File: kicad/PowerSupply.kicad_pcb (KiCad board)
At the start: 2 copper layers, 90 x 140 mm, 115 parts, among them J1 USB_A, J2 Display, Q1 MMBT3904, Q10 MMBT3904, Q11 MMBT3904, Q2 MMBT3904, Q3 MMBT3904, Q4 MMBT3904, Q5 MMBT3904, Q6 MMBT3904, Q7 MMBT3904, Q8 MMBT3904, Q9 MMBT3904, SW1 ENC0 (Voltage), SW2 ENC1 (Current), SW3 SW_DIP_x04, U1 OPA4196, U10 STM32F373C8Tx, U2 OPA4196, U3 LD1086D2T33, U4 LD1086D2T33, U5 FQA36P15, U6 FQA36P15, U7 FQA36P15, U8 FQA36P15

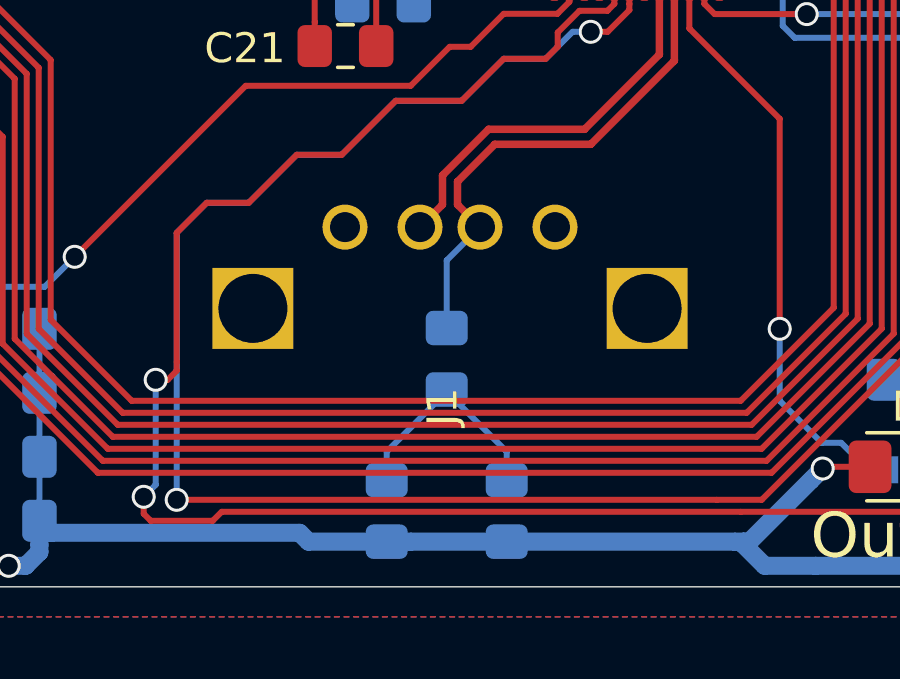
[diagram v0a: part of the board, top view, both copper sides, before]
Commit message: Fixed USB connector footprint, silkscreen was on mask layer
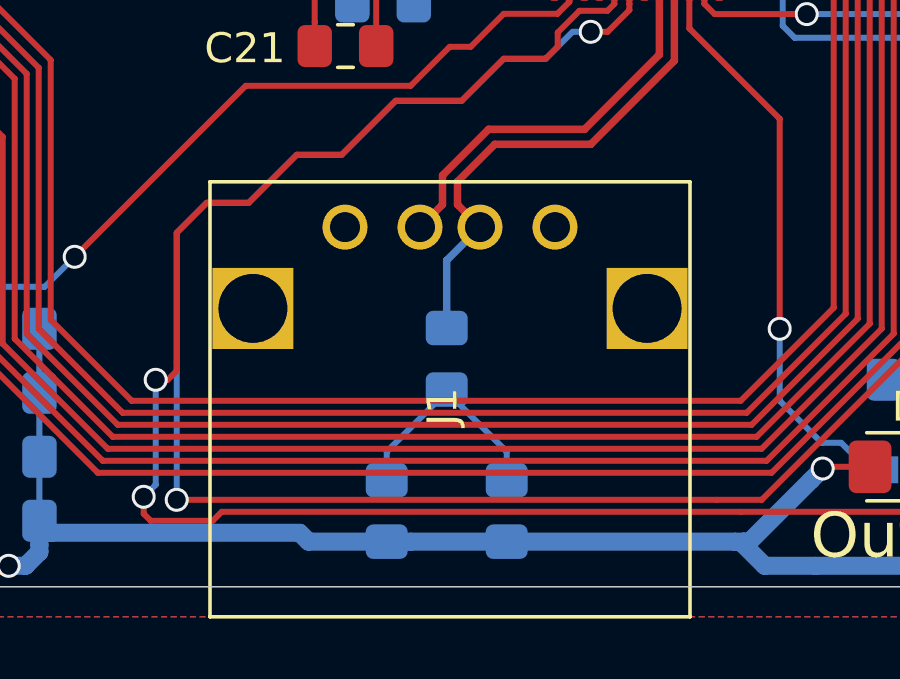
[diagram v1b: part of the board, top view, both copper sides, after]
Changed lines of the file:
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@@
       (effects (font (size 1 1) (thickness 0.15)))
     )
-    (fp_line (start 0 8) (end 14.5 8) (layer F.Mask) (width 0.12))
-    (fp_line (start 0 -8) (end 0 8) (layer F.Mask) (width 0.12))
-    (fp_line (start 14.5 -8) (end 0 -8) (layer F.Mask) (width 0.12))
-    (fp_line (start 14.5 -8) (end 14.5 8) (layer F.Mask) (width 0.12))
+    (fp_line (start 0 8) (end 14.5 8) (layer F.SilkS) (width 0.12))
+    (fp_line (start 0 -8) (end 0 8) (layer F.SilkS) (width 0.12))
+    (fp_line (start 14.5 -8) (end 0 -8) (layer F.SilkS) (width 0.12))
+    (fp_line (start 14.5 -8) (end 14.5 8) (layer F.SilkS) (width 0.12))
     (pad 4 thru_hole circle (at 12.99 3.5 90) (size 1.5 1.5) (drill 1) (layers *.Cu *.Mask)
       (net 1 GNDREF))
@@
   (segment (start 331.203554 125.25) (end 333.99 122.463554) (width 0.25) (layer F.Cu) (net 8))
   (segment (start 333.99 122.463554) (end 333.99 119.7325) (width 0.25) (layer F.Cu) (net 8))
-  (segment (start 326.4 129.12) (end 327.51 128.01) (width 0.2) (layer B.Cu) (net 8))
-  (segment (start 326.4 131.445) (end 326.4 129.12) (width 0.2) (layer B.Cu) (net 8))
+  (segment (start 326.4 129.12) (end 327.51 128.01) (width 0.25) (layer B.Cu) (net 8) (status 1000000))
+  (segment (start 326.4 131.445) (end 326.4 129.12) (width 0.25) (layer B.Cu) (net 8) (status 1000000))
   (segment (start 325.51 128.01) (end 326.26 127.26) (width 0.25) (layer F.Cu) (net 9))
   (segment (start 326.26 127.26) (end 326.26 126.286446) (width 0.25) (layer F.Cu) (net 9))
@@
   (segment (start 331.85 115.3) (end 333.8 113.35) (width 0.2) (layer F.Cu) (net 26))
   (segment (start 333.8 113.35) (end 334.2 113.35) (width 0.2) (layer F.Cu) (net 26))
-  (via (at 344.9 108) (size 0.8) (drill 0.6) (layers F.Cu B.Cu) (net 26) (status 1000000))
+  (via (at 344.9 108) (size 0.8) (drill 0.6) (layers F.Cu B.Cu) (net 26))
   (segment (start 344.825 108) (end 344.9 108) (width 0.2) (layer F.Cu) (net 26))
   (segment (start 329 92) (end 329 92.175) (width 0.2) (layer F.Cu) (net 26))

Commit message: git status
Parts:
- C1, C10, C11, C12, C13, C14, C15, C16, C17, C18, C19, C2, C20, C21, C22, C23, C24, C25, C26, C3, C4, C5, C6, C7, C8, C9: footprint Resistor_SMD:R_0805_2012Metric_Pad1.15x1.40mm_HandSolder -> Capacitor_SMD:C_0805_2012Metric_Pad1.15x1.40mm_HandSolder
- U5, U6, U7, U8: value FQA36P15 -> FQP17P10; footprint Package_TO_SOT_THT:TO-3P-3_Vertical -> Package_TO_SOT_THT:TO-220-3_Vertical
- moved U5 2.96 mm to (364.0, 105.5)
- moved U6 2.96 mm to (364.0, 47.5)
- moved U7 2.96 mm to (364.0, 76.5)
- moved U8 2.96 mm to (364.0, 18.5)
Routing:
- net /PassElement/Vin: track 270.4 -> 282.5 mm
- net /PassElement/Vout: track 326.9 -> 332.6 mm
- net /PassElement/VReg_set: track 110.3 -> 112.9 mm
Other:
- board text added: "Current"
- board text added: "Voltage"

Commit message: IDK what this is but the last commit message should've been FUCK I don't remember. BRUH
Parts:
- removed the REF** at (304.8, 26.5)
- removed the REF** at (304.8, 15.5)
- removed the REF** at (304.5, 4.50)
- added REF**: SolderWirePad_1x01_Drill2mm, Connector_Wire:SolderWirePad_1x01_Drill2mm, F.Cu at (4.75, 26.5)
- added REF**: SolderWirePad_1x01_Drill2mm, Connector_Wire:SolderWirePad_1x01_Drill2mm, F.Cu at (4.75, 15.5)
- added REF**: SolderWirePad_1x01_Drill2mm, Connector_Wire:SolderWirePad_1x01_Drill2mm, F.Cu at (4.50, 4.50)
- moved C1 300.0 mm to (31.0, 59.2)
- moved C10 300.0 mm to (67.0, 57.0)
- moved C11 300.0 mm to (10.0, 9.00)
- moved C12 300.0 mm to (39.8, 81.0)
- moved C13 300.0 mm to (30.3, 115.8)
- moved C14 300.0 mm to (32.7, 115.8)
- moved C15 300.0 mm to (35.1, 115.8)
- moved C16 300.0 mm to (24.2, 118.4)
- moved C17 300.0 mm to (24.2, 116.0)
- moved C18 300.0 mm to (24.3, 120.5)
- moved C19 300.0 mm to (23.0, 117.2)
- moved C2 300.0 mm to (31.0, 80.8)
- moved C20 300.0 mm to (23.0, 119.6)
- moved C21 300.0 mm to (23.0, 122.0)
- moved C22 300.0 mm to (37.6, 109.8)
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
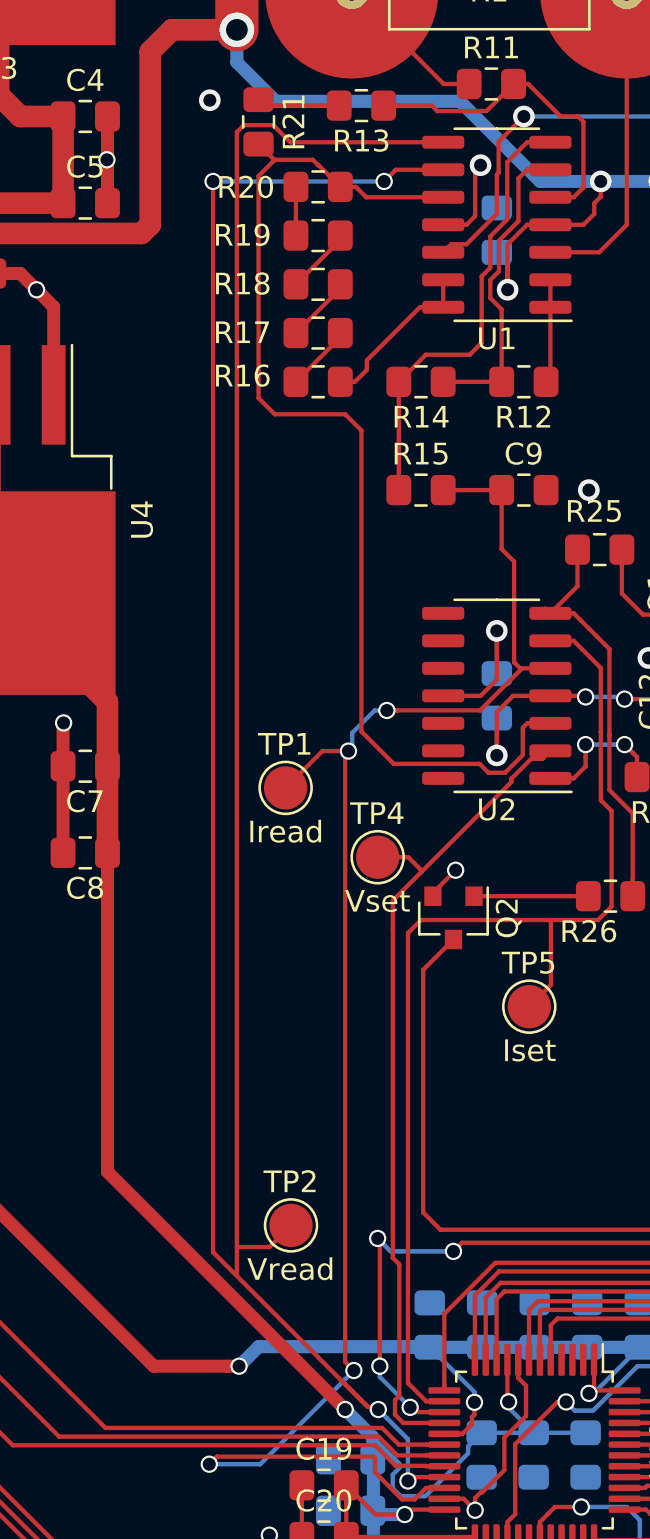
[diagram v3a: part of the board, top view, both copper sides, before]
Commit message: Removed unnecessary trace
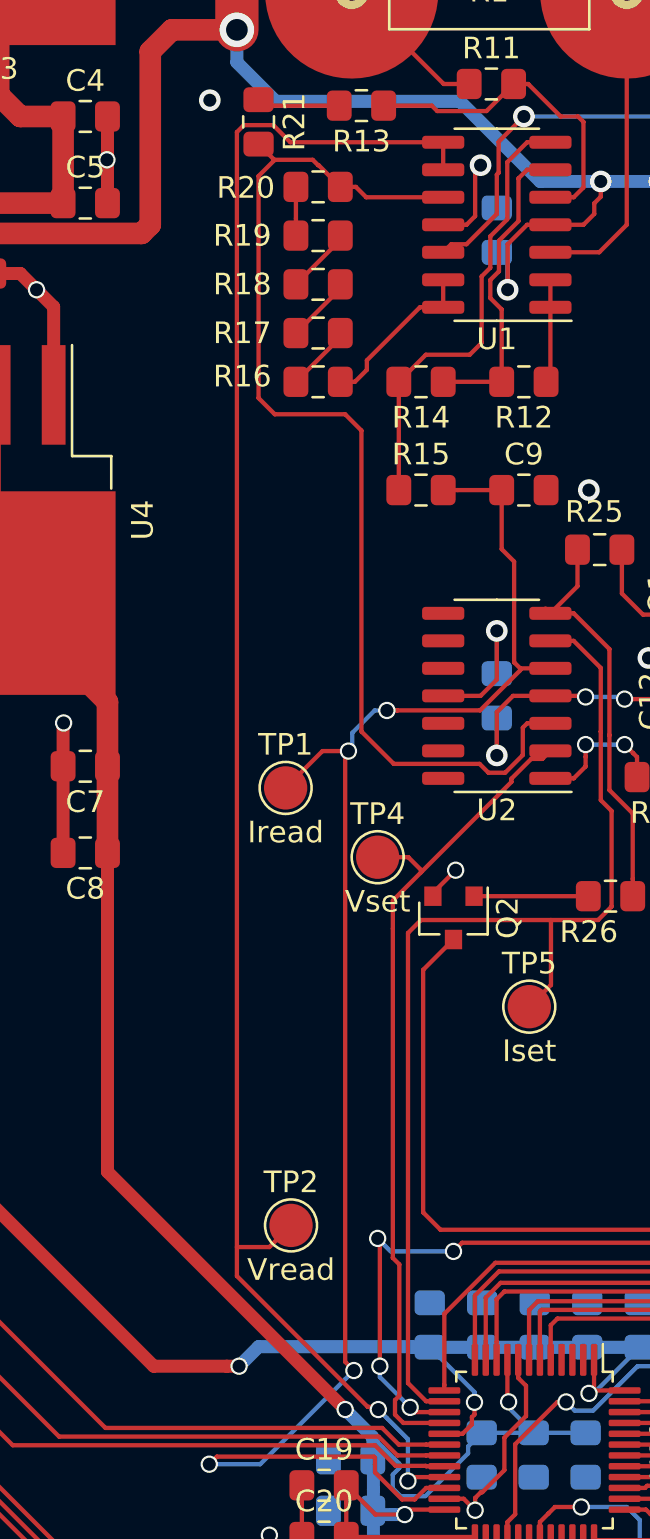
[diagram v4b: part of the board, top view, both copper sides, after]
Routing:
- net /Logic/Vread: track 144.3 -> 82.0 mm, vias 4 -> 2
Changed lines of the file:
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@@
     (thickness 1.6)
     (drawings 10)
-    (tracks 1118)
+    (tracks 1112)
     (zones 0)
     (modules 115)
@@
   (segment (start 46.565685 111.2) (end 46 111.2) (width 0.2) (layer F.Cu) (net 50))
   (segment (start 45.600001 111.599999) (end 46 111.2) (width 0.2) (layer B.Cu) (net 50))
-  (via (at 25.8 57) (size 0.8) (drill 0.6) (layers F.Cu B.Cu) (net 51))
-  (segment (start 28.525 56.46) (end 26.34 56.46) (width 0.2) (layer F.Cu) (net 51))
-  (segment (start 26.34 56.46) (end 25.8 57) (width 0.2) (layer F.Cu) (net 51))
-  (via (at 17.9 57) (size 0.8) (drill 0.6) (layers F.Cu B.Cu) (net 51))
-  (segment (start 25.8 57) (end 17.9 57) (width 0.2) (layer B.Cu) (net 51))
   (via (at 26.895722 116.99999) (size 0.8) (drill 0.6) (layers F.Cu B.Cu) (net 51))
   (segment (start 27.075712 116.82) (end 26.895722 116.99999) (width 0.2) (layer F.Cu) (net 51))
@@
   (segment (start 20.500001 106.199999) (end 18.99999 106.20001) (width 0.2) (layer F.Cu) (net 51))
   (segment (start 21.5 105.2) (end 20.500001 106.199999) (width 0.2) (layer F.Cu) (net 51))
-  (segment (start 19.322176 54.39999) (end 18.99999 54.722176) (width 0.2) (layer F.Cu) (net 51))
-  (segment (start 18.99999 54.722176) (end 18.99999 107.480728) (width 0.2) (layer F.Cu) (net 51))
-  (segment (start 17.9 106.436002) (end 25.042558 113.57856) (width 0.2) (layer F.Cu) (net 51))
-  (segment (start 20.677824 54.39999) (end 19.322176 54.39999) (width 0.2) (layer F.Cu) (net 51))
-  (segment (start 21.467834 55.19) (end 20.677824 54.39999) (width 0.2) (layer F.Cu) (net 51))
-  (segment (start 23.799999 112.336001) (end 25.042558 113.57856) (width 0.2) (layer F.Cu) (net 51))
-  (segment (start 28.525 55.19) (end 21.467834 55.19) (width 0.2) (layer F.Cu) (net 51))
-  (segment (start 17.9 57) (end 17.9 106.436002) (width 0.2) (layer F.Cu) (net 51))
+  (segment (start 28.525 56.46) (end 28.525 55.19) (width 0.2) (layer F.Cu) (net 51))
   (segment (start 25.407351 113.57856) (end 25.529329 113.700538) (width 0.2) (layer F.Cu) (net 51))
+  (segment (start 21.467834 55.19) (end 20.677824 54.39999) (width 0.2) (layer F.Cu) (net 51))
   (segment (start 25.042558 113.57856) (end 25.407351 113.57856) (width 0.2) (layer F.Cu) (net 51))
+  (segment (start 28.525 55.19) (end 21.467834 55.19) (width 0.2) (layer F.Cu) (net 51))
+  (segment (start 20.677824 54.39999) (end 19.322176 54.39999) (width 0.2) (layer F.Cu) (net 51))
+  (segment (start 19.322176 54.39999) (end 18.99999 54.722176) (width 0.2) (layer F.Cu) (net 51))
+  (segment (start 18.99999 54.722176) (end 18.99999 107.535992) (width 0.2) (layer F.Cu) (net 51))
+  (segment (start 18.99999 107.535992) (end 25.042558 113.57856) (width 0.2) (layer F.Cu) (net 51))
   (segment (start 33.485 78.2) (end 33.475 78.21) (width 0.2) (layer F.Cu) (net 52))
   (segment (start 34.55 78.21) (end 33.475 78.21) (width 0.2) (layer F.Cu) (net 52))
@@
     (connect_pads (clearance 0.2))
     (min_thickness 0.25)
-    (fill yes (arc_segments 32) (thermal_gap 0.508) (thermal_bridge_width 0.254))
+    (fill (arc_segments 32) (thermal_gap 0.508) (thermal_bridge_width 0.254))
     (polygon
       (pts
@@
     (connect_pads (clearance 0.2))
     (min_thickness 0.25)
-    (fill yes (arc_segments 32) (thermal_gap 0.508) (thermal_bridge_width 0.254))
+    (fill (arc_segments 32) (thermal_gap 0.508) (thermal_bridge_width 0.254))
     (polygon
       (pts

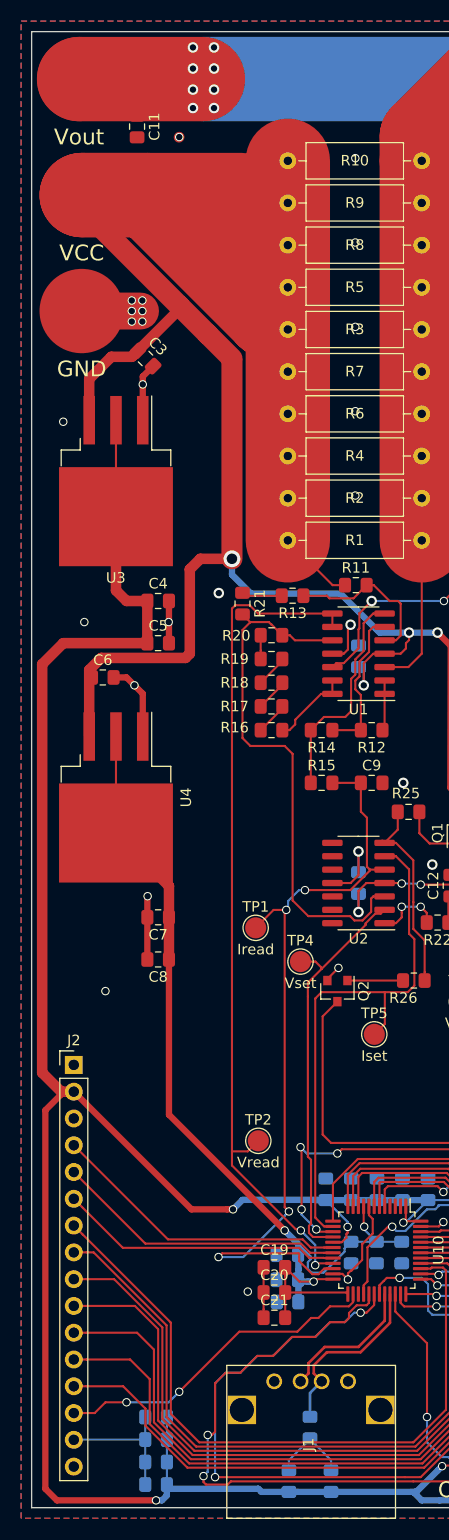
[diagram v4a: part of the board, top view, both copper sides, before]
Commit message: Added OSH symbol
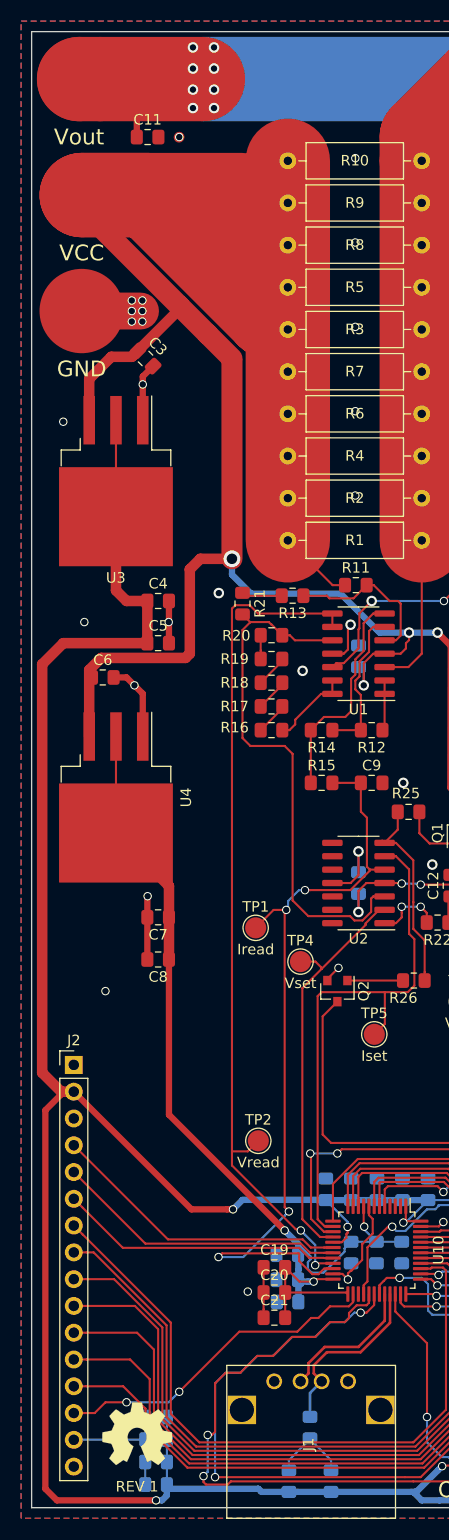
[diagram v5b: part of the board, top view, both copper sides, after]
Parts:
- added REF**: OSHW-Symbol_6.7x6mm_SilkScreen, Symbol:OSHW-Symbol_6.7x6mm_SilkScreen, F.Cu at (10.0, 133.0)
- moved C11 1.41 mm to (11.0, 10.0), turned to 0 degrees
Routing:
- net /PassElement/Vout: track 332.6 -> 339.5 mm
- net /Logic/CODE_B0: track 70.6 -> 68.2 mm, vias 6 -> 4
- net GNDREF: vias 42 -> 43
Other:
- board text added: "REV 1"

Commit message: I think this is it, it's complete
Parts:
- R22, R23, R24: value 1k -> ?
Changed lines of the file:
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@@
     (add_net VDD)
   )
-  (module Symbol:OSHW-Symbol_6.7x6mm_SilkScreen (layer F.Cu)
+  (module Symbol:OSHW-Symbol_6.7x6mm_SilkScreen locked (layer F.Cu)
     (at 10 133)
     (descr "Open Source Hardware Symbol")
@@
     )
   )
-  (module Connector_Wire:SolderWirePad_1x01_Drill2mm (layer F.Cu)
+  (module Connector_Wire:SolderWirePad_1x01_Drill2mm locked (layer F.Cu)
     (at 4.75 26.5)
     (descr "Wire solder connection")
@@
       (net 1 GNDREF))
   )
-  (module Connector_Wire:SolderWirePad_1x01_Drill2mm (layer F.Cu)
+  (module Connector_Wire:SolderWirePad_1x01_Drill2mm locked (layer F.Cu)
     (at 4.75 15.5)
     (descr "Wire solder connection")
@@
       (net 2 VDD))
   )
-  (module Connector_Wire:SolderWirePad_1x01_Drill2mm (layer F.Cu)
+  (module Connector_Wire:SolderWirePad_1x01_Drill2mm locked (layer F.Cu)
     (at 4.5 4.5)
     (descr "Wire solder connection")
@@
       (effects (font (size 1 1) (thickness 0.15)))
     )
-    (fp_text value 1k (at 0 1.65 90) (layer F.Fab)
+    (fp_text value ? (at 0 1.65 90) (layer F.Fab)
       (effects (font (size 1 1) (thickness 0.15)))
     )
@@
       (effects (font (size 1 1) (thickness 0.15)))
     )
-    (fp_text value 1k (at 0 1.65 90) (layer F.Fab)
+    (fp_text value ? (at 0 1.65 90) (layer F.Fab)
       (effects (font (size 1 1) (thickness 0.15)))
     )
@@
       (effects (font (size 1 1) (thickness 0.15)))
     )
-    (fp_text value 1k (at 0 1.65) (layer F.Fab)
+    (fp_text value ? (at 0 1.65) (layer F.Fab)
       (effects (font (size 1 1) (thickness 0.15)))
     )
@@
     (connect_pads (clearance 0.2))
     (min_thickness 0.25)
-    (fill (arc_segments 32) (thermal_gap 0.508) (thermal_bridge_width 0.254))
+    (fill yes (arc_segments 32) (thermal_gap 0.508) (thermal_bridge_width 0.254))
     (polygon
       (pts
@@
     (connect_pads (clearance 0.2))
     (min_thickness 0.25)
-    (fill (arc_segments 32) (thermal_gap 0.508) (thermal_bridge_width 0.254))
+    (fill yes (arc_segments 32) (thermal_gap 0.508) (thermal_bridge_width 0.254))
     (polygon
       (pts
